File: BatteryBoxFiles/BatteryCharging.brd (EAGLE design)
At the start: 36.1 x 59.6 mm, 3 parts, among them X1 MAB5SV, X2 MAB5SV

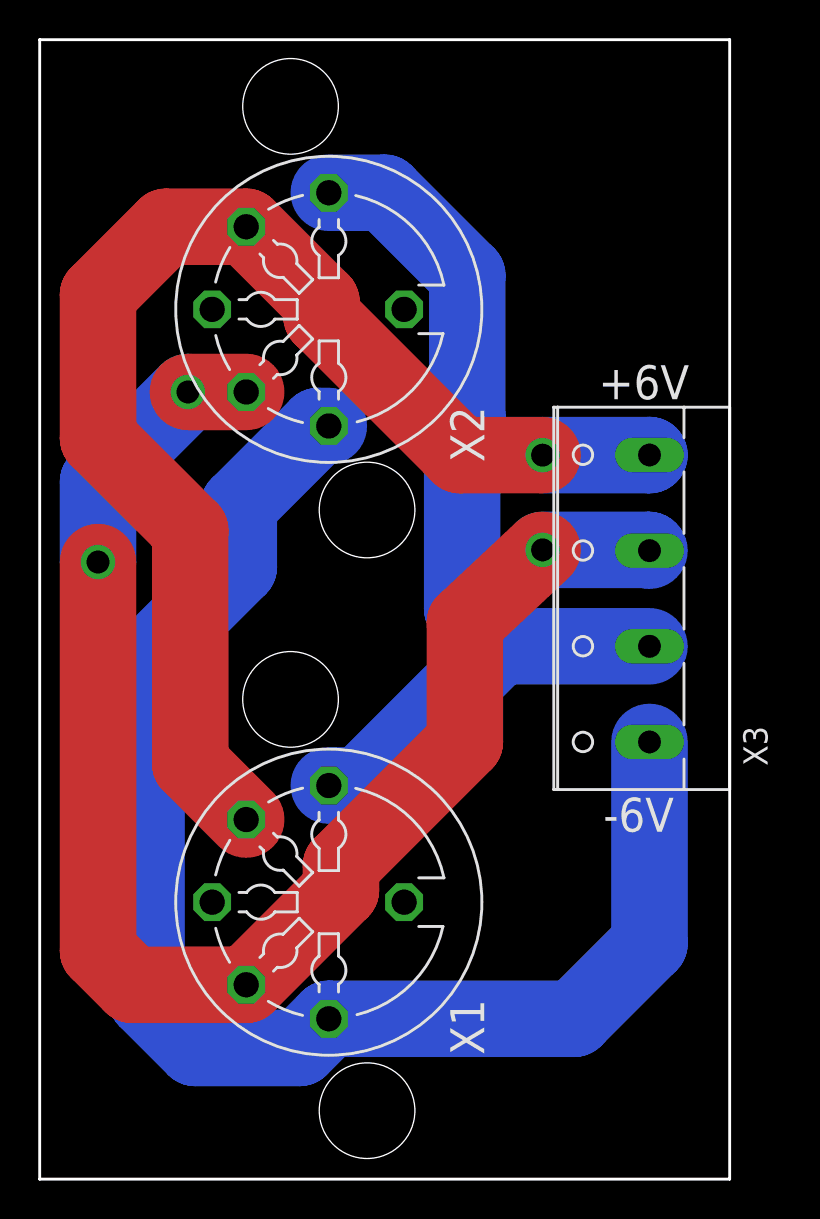
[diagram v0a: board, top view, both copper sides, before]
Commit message: Changed name of repository and added voltage source files
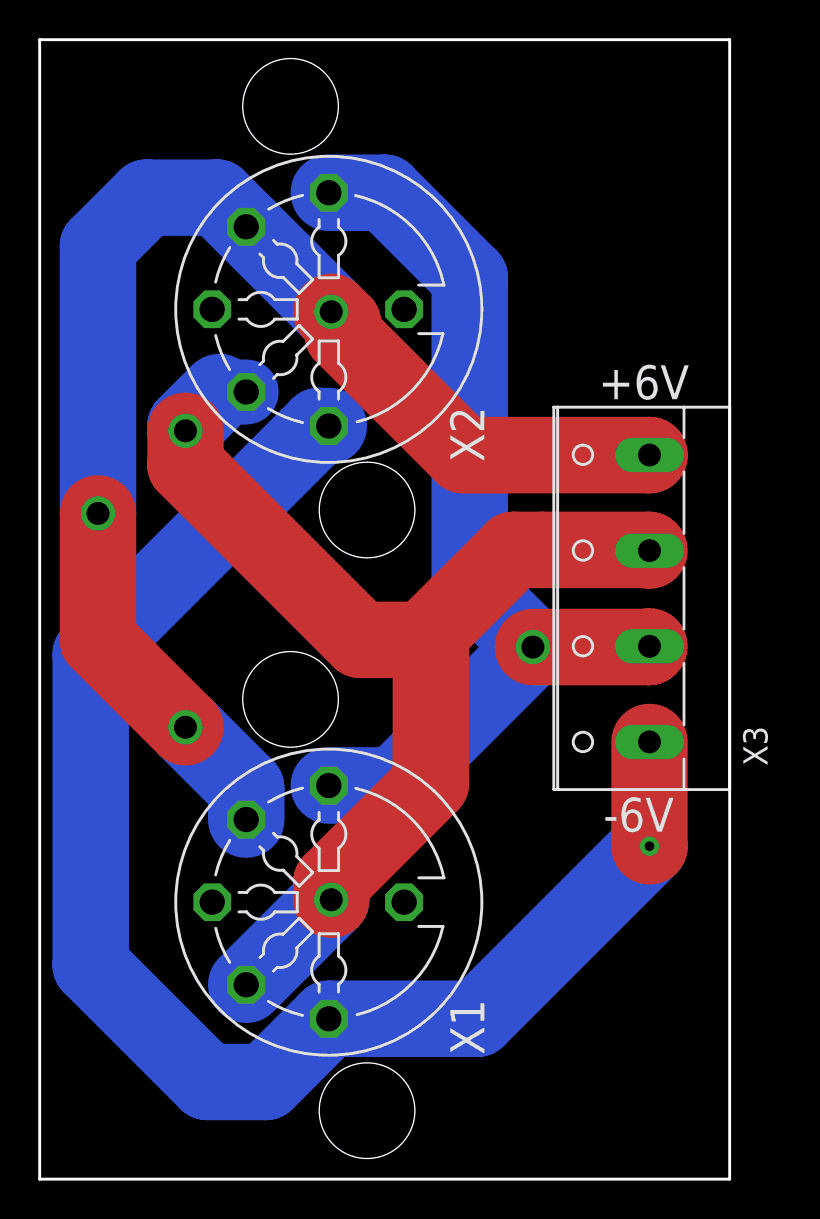
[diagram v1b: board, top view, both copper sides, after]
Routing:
- net +0V: track 77.5 -> 58.2 mm, vias 3 -> 2
- net +6V: track 66.3 -> 69.0 mm, vias 1 -> 3
- net -6V: track 74.4 -> 75.9 mm, vias 0 -> 1
- net -0V: track 49.1 -> 49.7 mm, vias 0 -> 1
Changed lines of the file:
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@@
 <contactref element="X2" pad="3"/>
 <contactref element="X3" pad="2"/>
-<wire x1="29.845" y1="31.496" x2="31.496" y2="31.496" width="4" layer="16"/>
-<wire x1="46.609" y1="38.775" x2="38.775" y2="38.775" width="4" layer="16"/>
-<wire x1="31.496" y1="31.496" x2="38.775" y2="38.775" width="4" layer="16"/>
 <wire x1="29.845" y1="62.484" x2="32.766" y2="62.484" width="4" layer="16"/>
-<wire x1="32.766" y1="62.484" x2="37.084" y2="58.166" width="4" layer="16"/>
-<wire x1="37.084" y1="50.775225" x2="36.8178" y2="50.509025" width="4" layer="16"/>
-<wire x1="36.8178" y1="50.509025" x2="36.8178" y2="40.7322" width="4" layer="16"/>
-<wire x1="36.8178" y1="40.7322" x2="38.775" y2="38.775" width="4" layer="16"/>
-<wire x1="37.084" y1="58.166" x2="37.084" y2="50.775225" width="4" layer="16"/>
+<wire x1="32.766" y1="62.484" x2="37.211" y2="58.039" width="4" layer="16"/>
+<wire x1="33.274" y1="31.496" x2="40.513" y2="38.735" width="4" layer="16"/>
+<via x="40.513" y="38.735" extent="1-16" drill="1.2"/>
+<wire x1="40.513" y1="38.735" x2="46.569" y2="38.735" width="4" layer="1"/>
+<wire x1="46.569" y1="38.735" x2="46.609" y2="38.775" width="4" layer="1"/>
+<wire x1="29.845" y1="31.496" x2="33.274" y2="31.496" width="4" layer="16"/>
+<wire x1="37.211" y1="42.037" x2="40.513" y2="38.735" width="4" layer="16"/>
+<wire x1="37.211" y1="58.039" x2="37.211" y2="42.037" width="4" layer="16"/>
 </signal>
 <signal name="+6V">
@@
 <contactref element="X2" pad="5"/>
 <contactref element="X3" pad="4"/>
-<wire x1="25.527" y1="60.706" x2="21.336" y2="60.706" width="4" layer="1"/>
-<wire x1="21.336" y1="60.706" x2="17.78" y2="57.15" width="4" layer="1"/>
-<wire x1="17.78" y1="57.15" x2="17.78" y2="49.657" width="4" layer="1"/>
-<wire x1="17.78" y1="49.657" x2="22.6018" y2="44.8352" width="4" layer="1"/>
-<wire x1="22.6018" y1="32.6432" x2="25.527" y2="29.718" width="4" layer="1"/>
-<wire x1="22.6018" y1="44.8352" x2="22.6018" y2="32.6432" width="4" layer="1"/>
-<wire x1="25.527" y1="60.706" x2="29.464" y2="56.769" width="4" layer="1"/>
-<wire x1="29.464" y1="56.769" x2="29.464" y2="56.007" width="4" layer="1"/>
-<wire x1="36.703" y1="48.768" x2="41.021" y2="48.768" width="4" layer="1"/>
-<via x="41.021" y="48.768" extent="1-16" drill="1.2"/>
-<wire x1="41.021" y1="48.768" x2="46.602" y2="48.768" width="4" layer="16"/>
-<wire x1="46.602" y1="48.768" x2="46.609" y2="48.775" width="4" layer="16"/>
-<wire x1="29.464" y1="56.007" x2="36.703" y2="48.768" width="4" layer="1"/>
+<wire x1="25.527" y1="60.706" x2="24.003" y2="62.23" width="4" layer="16"/>
+<wire x1="20.32" y1="62.23" x2="24.003" y2="62.23" width="4" layer="16"/>
+<wire x1="25.527" y1="29.718" x2="25.527" y2="31.369" width="4" layer="16"/>
+<wire x1="25.527" y1="31.369" x2="22.352" y2="34.544" width="4" layer="16"/>
+<via x="22.352" y="34.544" extent="1-16" drill="1.2"/>
+<wire x1="22.352" y1="34.544" x2="17.78" y2="39.116" width="4" layer="1"/>
+<wire x1="17.78" y1="39.116" x2="17.78" y2="45.72" width="4" layer="1"/>
+<via x="17.78" y="45.72" extent="1-16" drill="1.2"/>
+<wire x1="17.78" y1="45.72" x2="17.78" y2="59.69" width="4" layer="16"/>
+<wire x1="17.78" y1="59.69" x2="20.32" y2="62.23" width="4" layer="16"/>
+<wire x1="25.527" y1="60.706" x2="29.972" y2="56.261" width="4" layer="16"/>
+<via x="29.972" y="56.261" extent="1-16" drill="1.2"/>
+<wire x1="29.972" y1="56.261" x2="30.5882" y2="55.6448" width="4" layer="1"/>
+<wire x1="30.5882" y1="55.6448" x2="30.5882" y2="55.06508125" width="4" layer="1"/>
+<wire x1="30.5882" y1="55.06508125" x2="36.88528125" y2="48.768" width="4" layer="1"/>
+<wire x1="46.602" y1="48.768" x2="46.609" y2="48.775" width="4" layer="1"/>
+<wire x1="36.88528125" y1="48.768" x2="46.602" y2="48.768" width="4" layer="1"/>
 </signal>
 <signal name="+0V">
@@
 <contactref element="X2" pad="4"/>
 <contactref element="X3" pad="3"/>
-<wire x1="19.558" y1="21.082" x2="17.78" y2="22.86" width="4" layer="1"/>
-<wire x1="25.527" y1="21.082" x2="19.558" y2="21.082" width="4" layer="1"/>
-<wire x1="25.527" y1="21.082" x2="30.48" y2="26.035" width="4" layer="1"/>
-<wire x1="30.48" y1="26.035" x2="30.48" y2="27.305" width="4" layer="1"/>
-<wire x1="30.48" y1="27.305" x2="36.957" y2="33.782" width="4" layer="1"/>
-<wire x1="17.78" y1="22.86" x2="17.78" y2="43.18" width="4" layer="1"/>
-<via x="17.78" y="43.18" extent="1-16" drill="1.2"/>
-<wire x1="17.78" y1="43.18" x2="17.78" y2="47.371" width="4" layer="16"/>
-<wire x1="17.78" y1="47.371" x2="22.479" y2="52.07" width="4" layer="16"/>
-<via x="22.479" y="52.07" extent="1-16" drill="1.2"/>
-<wire x1="22.479" y1="52.07" x2="25.527" y2="52.07" width="4" layer="1"/>
-<wire x1="36.957" y1="40.005" x2="41.021" y2="43.815" width="4" layer="1"/>
-<via x="41.021" y="43.815" extent="1-16" drill="1.2"/>
-<wire x1="41.021" y1="43.815" x2="46.569" y2="43.815" width="4" layer="16"/>
-<wire x1="46.569" y1="43.815" x2="46.609" y2="43.775" width="4" layer="16"/>
-<wire x1="36.957" y1="33.782" x2="36.957" y2="40.005" width="4" layer="1"/>
+<wire x1="25.527" y1="21.082" x2="29.972" y2="25.527" width="4" layer="16"/>
+<via x="29.972" y="25.527" extent="1-16" drill="1.2"/>
+<wire x1="29.972" y1="25.527" x2="29.972" y2="26.416" width="4" layer="1"/>
+<wire x1="35.179" y1="31.623" x2="35.179" y2="39.116" width="4" layer="1"/>
+<wire x1="35.179" y1="39.116" x2="35.179" y2="39.497" width="4" layer="1"/>
+<wire x1="35.179" y1="39.497" x2="39.497" y2="43.815" width="4" layer="1"/>
+<wire x1="39.497" y1="43.815" x2="41.021" y2="43.815" width="4" layer="1"/>
+<wire x1="29.972" y1="26.416" x2="35.179" y2="31.623" width="4" layer="1"/>
+<wire x1="25.527" y1="52.07" x2="24.13" y2="52.07" width="3.4" layer="16"/>
+<wire x1="24.13" y1="52.07" x2="22.352" y2="50.292" width="4" layer="16"/>
+<wire x1="22.352" y1="50.292" x2="22.352" y2="50.038" width="4" layer="16"/>
+<via x="22.352" y="50.038" extent="1-16" drill="1.2"/>
+<wire x1="35.179" y1="39.116" x2="31.496" y2="39.116" width="4" layer="1"/>
+<wire x1="22.352" y1="48.26" x2="22.352" y2="50.038" width="4" layer="1"/>
+<wire x1="31.496" y1="39.116" x2="22.352" y2="48.26" width="4" layer="1"/>
+<wire x1="41.021" y1="43.815" x2="46.569" y2="43.815" width="4" layer="1"/>
+<wire x1="46.569" y1="43.815" x2="46.609" y2="43.775" width="4" layer="1"/>
 </signal>
 <signal name="-6V">
@@
 <contactref element="X2" pad="1"/>
 <contactref element="X3" pad="1"/>
-<wire x1="29.845" y1="19.304" x2="28.321" y2="17.78" width="4" layer="16"/>
-<wire x1="28.321" y1="17.78" x2="22.86" y2="17.78" width="4" layer="16"/>
-<wire x1="22.86" y1="17.78" x2="20.32" y2="20.32" width="4" layer="16"/>
-<wire x1="25.1418" y1="42.9218" x2="25.1418" y2="46.14413125" width="4" layer="16"/>
-<wire x1="20.32" y1="20.32" x2="20.32" y2="38.1" width="4" layer="16"/>
-<wire x1="20.32" y1="38.1" x2="25.1418" y2="42.9218" width="4" layer="16"/>
-<wire x1="25.1418" y1="46.14413125" x2="29.28966875" y2="50.292" width="4" layer="16"/>
-<wire x1="29.28966875" y1="50.292" x2="29.845" y2="50.292" width="4" layer="16"/>
-<wire x1="29.845" y1="19.304" x2="42.672" y2="19.304" width="4" layer="16"/>
-<wire x1="42.672" y1="19.304" x2="46.609" y2="23.241" width="4" layer="16"/>
-<wire x1="46.609" y1="23.241" x2="46.609" y2="33.775" width="4" layer="16"/>
+<wire x1="29.337" y1="50.292" x2="17.399" y2="38.354" width="4" layer="16"/>
+<wire x1="29.845" y1="19.304" x2="37.592" y2="19.304" width="4" layer="16"/>
+<wire x1="29.845" y1="50.292" x2="29.337" y2="50.292" width="4" layer="16"/>
+<wire x1="29.845" y1="19.304" x2="26.543" y2="16.002" width="4" layer="16"/>
+<wire x1="26.543" y1="16.002" x2="23.495" y2="16.002" width="4" layer="16"/>
+<wire x1="23.495" y1="16.002" x2="17.399" y2="22.098" width="4" layer="16"/>
+<wire x1="17.399" y1="22.098" x2="17.399" y2="38.354" width="4" layer="16"/>
+<wire x1="37.592" y1="19.304" x2="46.609" y2="28.321" width="4" layer="16"/>
+<via x="46.609" y="28.321" extent="1-16" drill="0.508"/>
+<wire x1="46.609" y1="28.321" x2="46.609" y2="33.775" width="4" layer="1"/>
 </signal>
 <signal name="GND">
